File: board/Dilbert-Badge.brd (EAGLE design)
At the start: 106.7 x 52.1 mm, 47 parts, among them IC1 MCP23017SO, J1 IO EXP., J2 FTDI_DEVICE, J3 NEOPIXEL, J4 PWR IN, J5 I2C, SW1 UP, SW2 DOWN, SW3 LEFT, SW4 RIGHT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

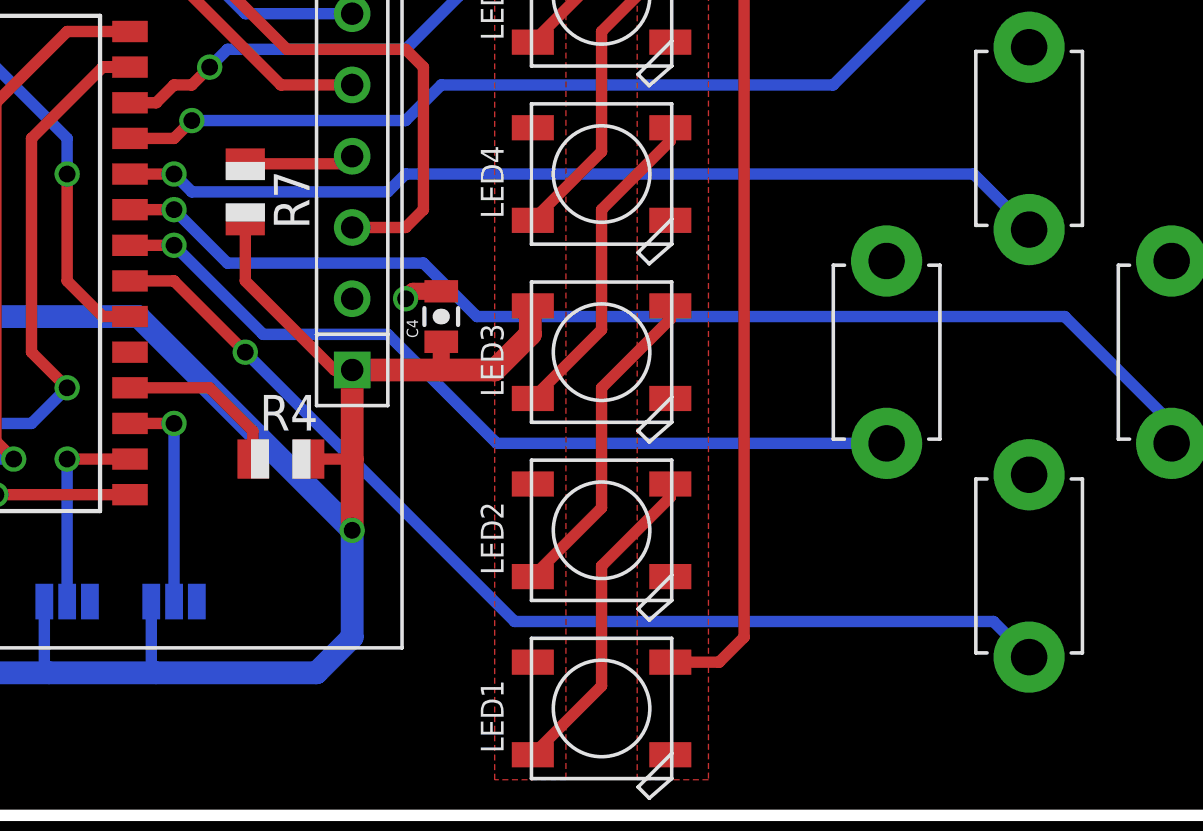
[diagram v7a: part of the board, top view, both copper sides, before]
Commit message: swap left/right buttons
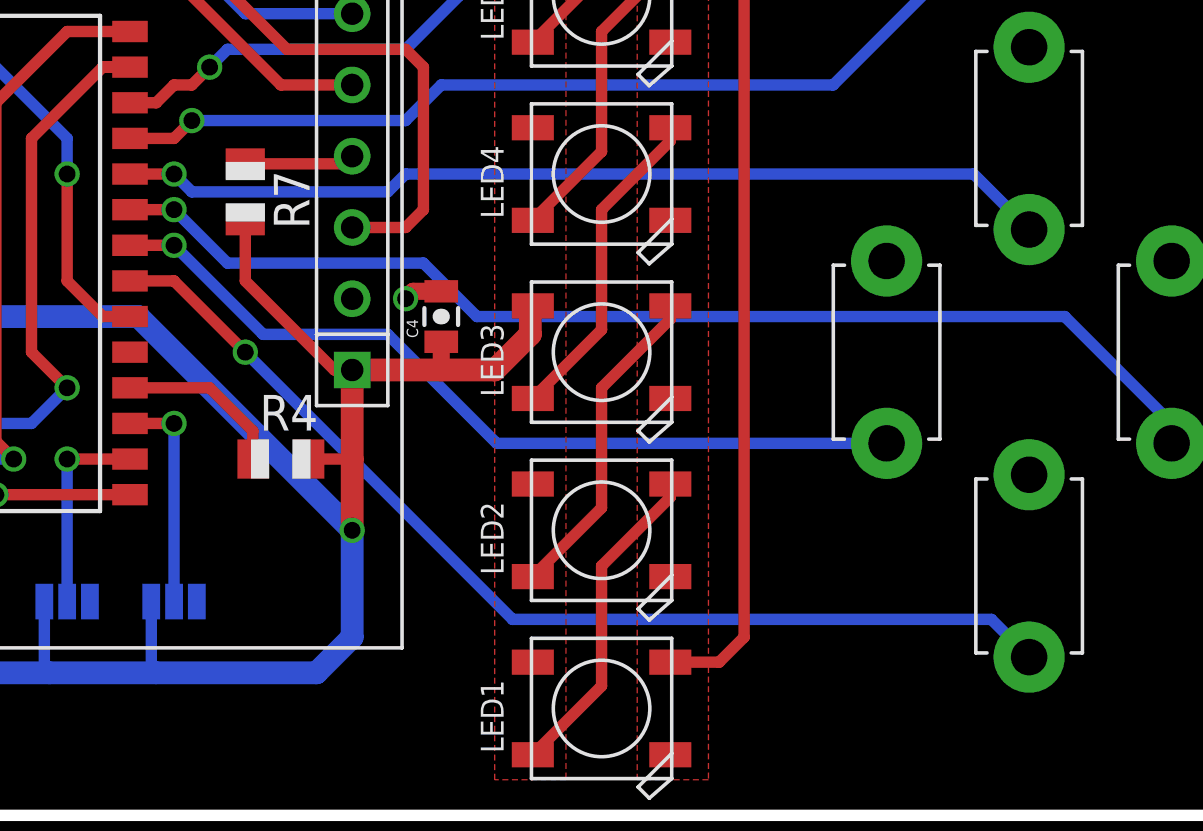
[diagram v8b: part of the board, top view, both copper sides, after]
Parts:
- moved SW3 15.2 mm to (90.2, 14.0)
- moved SW4 15.2 mm to (90.2, 29.2)
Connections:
- net BTN_L: now also IC1.21; no longer IC1.24
- net BTN_R: now also IC1.24; no longer IC1.21
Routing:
- net BTN_L: track 33.4 -> 37.6 mm
- net BTN_R: track 37.6 -> 33.4 mm
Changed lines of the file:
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@@
 <attribute name="VALUE" x="92.164" y="24.606" size="0.8128" layer="27" ratio="10" rot="R270"/>
 </element>
-<element name="SW3" library="adafruit" package="TACT_PANA-EVQ" value="LEFT" x="90.17" y="29.21" smashed="yes" rot="R270">
+<element name="SW3" library="adafruit" package="TACT_PANA-EVQ" value="LEFT" x="90.17" y="13.97" smashed="yes" rot="R270">
+<attribute name="VALUE" x="87.084" y="16.986" size="0.8128" layer="27" ratio="10" rot="R270"/>
+</element>
+<element name="SW4" library="adafruit" package="TACT_PANA-EVQ" value="RIGHT" x="90.17" y="29.21" smashed="yes" rot="R270">
 <attribute name="VALUE" x="87.084" y="32.226" size="0.8128" layer="27" ratio="10" rot="R270"/>
-</element>
-<element name="SW4" library="adafruit" package="TACT_PANA-EVQ" value="RIGHT" x="90.17" y="13.97" smashed="yes" rot="R270">
-<attribute name="VALUE" x="87.084" y="16.986" size="0.8128" layer="27" ratio="10" rot="R270"/>
 </element>
 <element name="SW5" library="adafruit" package="TACT_PANA-EVQ" value="A" x="92.71" y="40.64" smashed="yes" rot="R270">
@@
 <signal name="BTN_L">
 <contactref element="SW3" pad="P$2"/>
-<wire x1="88.19" y1="27.94" x2="67.945" y2="27.94" width="0.4064" layer="16"/>
-<wire x1="67.945" y1="27.94" x2="67.31" y2="27.305" width="0.4064" layer="16"/>
-<wire x1="67.31" y1="27.305" x2="60.325" y2="27.305" width="0.4064" layer="16"/>
-<wire x1="60.325" y1="27.305" x2="59.69" y2="27.94" width="0.4064" layer="16"/>
-<wire x1="88.19" y1="27.94" x2="90.17" y2="25.96" width="0.4064" layer="16"/>
-<contactref element="IC1" pad="24"/>
-<wire x1="58.12" y1="27.94" x2="59.69" y2="27.94" width="0.4064" layer="1"/>
-<via x="59.69" y="27.94" extent="1-16" drill="0.6"/>
-</signal>
-<signal name="BTN_R">
-<contactref element="SW4" pad="P$2"/>
-<wire x1="71.83" y1="11.99" x2="88.9" y2="11.99" width="0.4064" layer="16"/>
-<wire x1="88.9" y1="11.99" x2="90.17" y2="10.72" width="0.4064" layer="16"/>
 <contactref element="IC1" pad="21"/>
 <wire x1="58.12" y1="24.13" x2="59.69" y2="24.13" width="0.4064" layer="1"/>
 <wire x1="59.69" y1="24.13" x2="62.23" y2="21.59" width="0.4064" layer="1"/>
 <via x="62.23" y="21.59" extent="1-16" drill="0.6"/>
-<wire x1="62.23" y1="21.59" x2="71.83" y2="11.99" width="0.4064" layer="16"/>
+<wire x1="62.23" y1="21.59" x2="71.755" y2="12.065" width="0.4064" layer="16"/>
+<wire x1="71.755" y1="12.065" x2="88.825" y2="12.065" width="0.4064" layer="16"/>
+<wire x1="88.825" y1="12.065" x2="90.17" y2="10.72" width="0.4064" layer="16"/>
+</signal>
+<signal name="BTN_R">
+<contactref element="SW4" pad="P$2"/>
+<contactref element="IC1" pad="24"/>
+<wire x1="58.12" y1="27.94" x2="59.69" y2="27.94" width="0.4064" layer="1"/>
+<via x="59.69" y="27.94" extent="1-16" drill="0.6"/>
+<wire x1="59.69" y1="27.94" x2="60.325" y2="27.305" width="0.4064" layer="16"/>
+<wire x1="60.325" y1="27.305" x2="67.31" y2="27.305" width="0.4064" layer="16"/>
+<wire x1="67.31" y1="27.305" x2="67.945" y2="27.94" width="0.4064" layer="16"/>
+<wire x1="67.945" y1="27.94" x2="88.19" y2="27.94" width="0.4064" layer="16"/>
+<wire x1="88.19" y1="27.94" x2="90.17" y2="25.96" width="0.4064" layer="16"/>
 </signal>
 <signal name="BTN_A">
